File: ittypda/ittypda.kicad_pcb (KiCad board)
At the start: 2 copper layers, 105 x 109.8 mm, 172 parts, among them CN1 S2B-PH-SM4-TB, J1 USB_C_Receptacle_USB2.0_14P, J13 Conn_01x05_Pin, J14 Conn_01x05_Pin, J2 Conn_01x04_Pin, SW1 Switch, SW10 Switch, SW11 Switch, SW12 Switch, SW13 Switch, SW14 Switch, SW15 Switch, SW16 Switch, SW17 Switch, SW18 Switch, SW19 Switch, SW2 Switch, SW20 Switch, SW21 Switch, SW22 Switch, SW23 Switch, SW24 Switch, SW25 SLIDE SWITCH, SW26 Switch, SW27 Switch, SW28 Switch, SW29 Switch, SW3 Switch, SW30 Switch, SW31 Switch, SW32 Switch, SW33 Switch, SW34 Switch, SW36 Switch, SW37 Switch, SW38 Switch, SW39 Switch, SW4 Switch, SW41 Switch, SW42 Switch, SW43 Switch, SW44 Switch, SW45 Switch, SW46 Switch, SW47 Switch, SW48 Switch, SW49 Switch, SW5 Switch, SW50 Switch, SW51 Switch, SW52 Switch, SW53 Switch, SW54 Switch, SW55 Switch, SW56 Switch, SW57 Switch, SW58 Switch, SW59 Switch, SW6 Switch, SW60 Switch, SW61 Switch, SW7 Switch, SW8 Switch, SW9 Switch, U1 TPS63001, U2 BQ24040DSQR, U4 STM32F411RETx, Y1 16Mhz

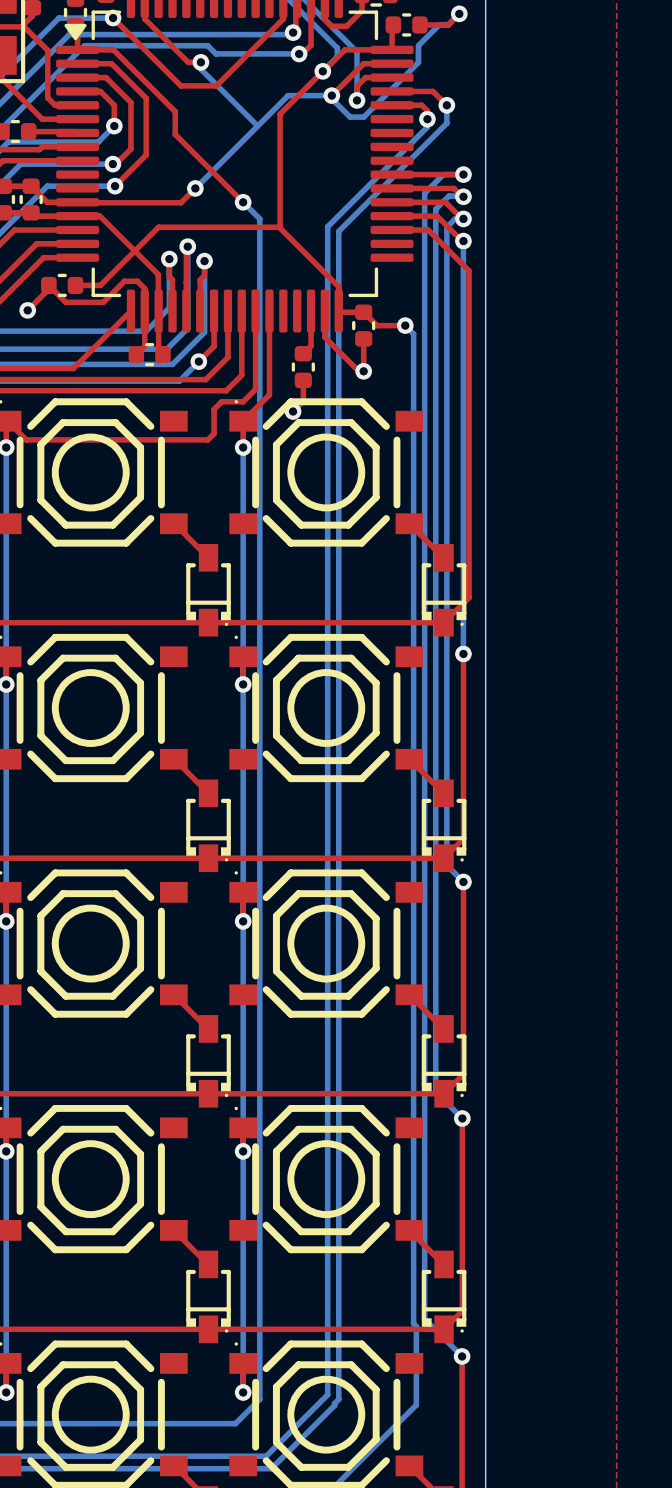
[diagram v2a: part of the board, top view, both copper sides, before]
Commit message: reorder row pins to reduce sharp angles
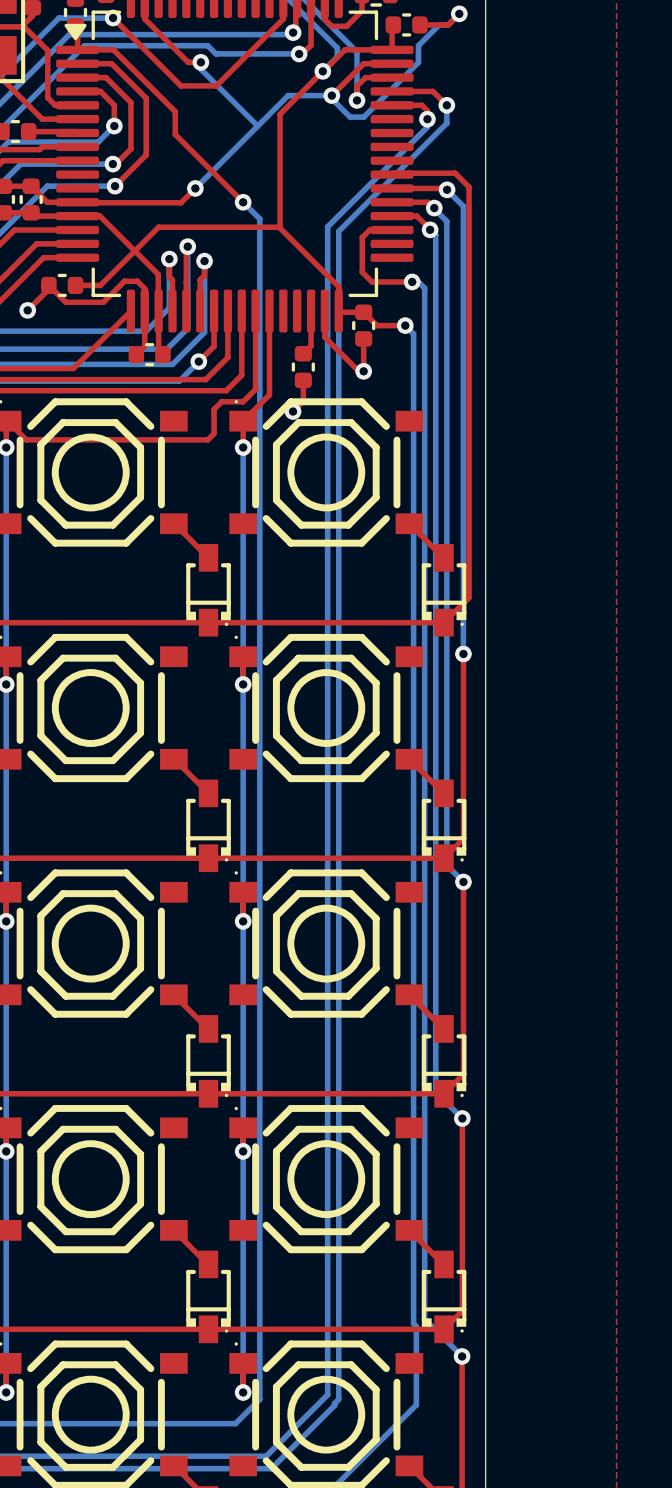
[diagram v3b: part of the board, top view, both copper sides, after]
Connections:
- U4 pad 35: Row0 -> Row4
- U4 pad 36: Row1 -> Row3
- U4 pad 38: Row3 -> Row1
- U4 pad 39: Row4 -> Row0
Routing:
- net Row3: track 138.6 -> 135.5 mm
- net Row0: track 110.0 -> 112.6 mm
- net Row4: track 147.8 -> 145.3 mm
- net Row1: track 119.0 -> 120.2 mm
- net Row2: track 128.9 -> 127.8 mm
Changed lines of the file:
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@@
 			(layers "F.Cu" "F.Mask" "F.Paste")
 			(roundrect_rratio 0.25)
-			(net "Row0")
+			(net "Row4")
 			(pinfunction "PB14_35")
 			(pintype "bidirectional")
@@
 			(layers "F.Cu" "F.Mask" "F.Paste")
 			(roundrect_rratio 0.25)
-			(net "Row1")
+			(net "Row3")
 			(pinfunction "PB15_36")
 			(pintype "bidirectional")
@@
 			(layers "F.Cu" "F.Mask" "F.Paste")
 			(roundrect_rratio 0.25)
-			(net "Row3")
+			(net "Row1")
 			(pinfunction "PC7_38")
 			(pintype "bidirectional")
@@
 			(layers "F.Cu" "F.Mask" "F.Paste")
 			(roundrect_rratio 0.25)
-			(net "Row4")
+			(net "Row0")
 			(pinfunction "PC8_39")
 			(pintype "bidirectional")
@@
 	)
 	(segment
+		(start 128.4 55.52)
+		(end 128.4 40.69964)
+		(width 0.2)
+		(layer "F.Cu")
+		(net "Row0")
+	)
+	(segment
 		(start 42.5 56.42)
 		(end 127.5 56.42)
@@
 	)
 	(segment
-		(start 128.4 55.52)
-		(end 128.4 43.725)
+		(start 127.5 56.42)
+		(end 128.4 55.52)
 		(width 0.2)
 		(layer "F.Cu")
@@
 	)
 	(segment
-		(start 126.925 42.25)
-		(end 125.625 42.25)
+		(start 125.675 40.2)
+		(end 125.625 40.25)
 		(width 0.2)
 		(layer "F.Cu")
@@
 	)
 	(segment
-		(start 128.4 43.725)
-		(end 126.925 42.25)
+		(start 127.90036 40.2)
+		(end 125.675 40.2)
 		(width 0.2)
 		(layer "F.Cu")
@@
 	)
 	(segment
-		(start 127.5 56.42)
-		(end 128.4 55.52)
+		(start 128.4 40.69964)
+		(end 127.90036 40.2)
 		(width 0.2)
 		(layer "F.Cu")
@@
 	)
 	(segment
-		(start 128.159823 81.260177)
-		(end 128.159823 74.312443)
-		(width 0.2)
-		(layer "F.Cu")
-		(net "Row3")
-	)
-	(segment
-		(start 127.851471 40.75)
-		(end 125.625 40.75)
+		(start 126.522013 41.75)
+		(end 125.625 41.75)
 		(width 0.2)
 		(layer "F.Cu")
@@
 	)
 	(segment
-		(start 127.5 81.92)
-		(end 128.159823 81.260177)
+		(start 127 42.240408)
+		(end 127 42.227987)
 		(width 0.2)
 		(layer "F.Cu")
@@
 	)
 	(segment
-		(start 128.2 41.050003)
-		(end 128.151474 41.050003)
+		(start 128.159823 81.260177)
+		(end 128.159823 74.312443)
 		(width 0.2)
 		(layer "F.Cu")
@@
 	)
 	(segment
-		(start 128.151474 41.050003)
-		(end 127.851471 40.75)
+		(start 127.5 81.92)
+		(end 128.159823 81.260177)
 		(width 0.2)
 		(layer "F.Cu")
@@
 	)
 	(segment
-		(start 128.2 41.050003)
-		(end 128.151476 41.098527)
+		(start 127 42.227987)
+		(end 126.522013 41.75)
 		(width 0.2)
 		(layer "F.Cu")
@@
 	)
 	(segment
-		(start 128.151476 41.098527)
-		(end 128.101473 41.098527)
+		(start 126.996599 42.243809)
+		(end 127 42.240408)
 		(width 0.2)
 		(layer "F.Cu")
@@
 	)
 	(via
-		(at 128.2 41.050003)
+		(at 126.996599 42.243809)
 		(size 0.6)
 		(drill 0.3)
@@
 	)
 	(segment
-		(start 127.675 41.025)
-		(end 128.174997 41.025)
+		(start 126.997244 42.244454)
+		(end 127.016467 42.244454)
 		(width 0.2)
 		(layer "B.Cu")
@@
 	)
 	(segment
-		(start 128.159823 74.312443)
+		(start 127.2 42.427987)
 		(end 127.2 73.35262)
 		(width 0.2)
@@
 	(segment
 		(start 127.2 73.35262)
-		(end 127.2 41.5)
+		(end 128.159823 74.312443)
 		(width 0.2)
 		(layer "B.Cu")
@@
 	)
 	(segment
-		(start 128.174997 41.025)
-		(end 128.2 41.050003)
+		(start 126.996599 42.243809)
+		(end 126.997244 42.244454)
 		(width 0.2)
 		(layer "B.Cu")
@@
 	)
 	(segment
-		(start 127.2 41.5)
-		(end 127.675 41.025)
+		(start 127.016467 42.244454)
+		(end 127.2 42.427987)
 		(width 0.2)
 		(layer "B.Cu")
@@
 	)
 	(segment
-		(start 128.2 40.25)
-		(end 125.8875 40.25)
+		(start 124.81759 42.25)
+		(end 125.625 42.25)
 		(width 0.2)
 		(layer "F.Cu")
@@
 	)
 	(segment
+		(start 124.55 42.51759)
+		(end 124.81759 42.25)
+		(width 0.2)
+		(layer "F.Cu")
+		(net "Row4")
+	)
+	(segment
 		(start 127.5 90.42)
 		(end 34 90.42)
@@
 		(net "Row4")
 	)
+	(segment
+		(start 124.55 43.775)
+		(end 124.55 42.51759)
+		(width 0.2)
+		(layer "F.Cu")
+		(net "Row4")
+	)
+	(segment
+		(start 126.35 44.125)
+		(end 124.9 44.125)
+		(width 0.2)
+		(layer "F.Cu")
+		(net "Row4")
+	)
+	(segment
+		(start 124.9 44.125)
+		(end 124.55 43.775)
+		(width 0.2)
+		(layer "F.Cu")
+		(net "Row4")
+	)
 	(via
 		(at 128.15 82.9)
@@
 	)
 	(via
-		(at 128.2 40.25)
+		(at 126.35 44.125)
 		(size 0.6)
 		(drill 0.3)
@@
 	)
 	(segment
-		(start 126.8 40.925)
-		(end 126.8 81.55)
+		(start 126.625 44.175)
+		(end 126.8 44.35)
 		(width 0.2)
 		(layer "B.Cu")
@@
 	)
 	(segment
-		(start 127.475 40.25)
-		(end 126.8 40.925)
+		(start 126.35 44.125)
+		(end 126.4 44.175)
 		(width 0.2)
 		(layer "B.Cu")
@@
 	)
 	(segment
-		(start 128.2 40.25)
-		(end 127.475 40.25)
+		(start 126.8 81.55)
+		(end 128.15 82.9)
 		(width 0.2)
 		(layer "B.Cu")
@@
 	)
 	(segment
-		(start 126.8 81.55)
-		(end 128.15 82.9)
+		(start 126.4 44.175)
+		(end 126.625 44.175)
+		(width 0.2)
+		(layer "B.Cu")
+		(net "Row4")
+	)
+	(segment
+		(start 126.8 44.35)
+		(end 126.8 81.55)
 		(width 0.2)
 		(layer "B.Cu")
@@
 	)
 	(segment
-		(start 127.551468 41.25)
-		(end 125.625 41.25)
+		(start 127.119089 41.458156)
+		(end 126.910933 41.25)
 		(width 0.2)
 		(layer "F.Cu")
@@
 	)
 	(segment
-		(start 128.151474 41.850006)
-		(end 127.551468 41.25)
+		(start 127.147443 41.458156)
+		(end 127.119089 41.458156)
 		(width 0.2)
 		(layer "F.Cu")
@@
 	)
 	(segment
-		(start 128.2 41.850006)
-		(end 128.151474 41.850006)
+		(start 127.5 73.42)
+		(end 34 73.42)
 		(width 0.2)
 		(layer "F.Cu")
@@
 	)
 	(segment
-		(start 127.5 73.42)
-		(end 34 73.42)
+		(start 126.910933 41.25)
+		(end 125.625 41.25)
 		(width 0.2)
 		(layer "F.Cu")
@@
 	)
 	(via
-		(at 128.2 41.850006)
+		(at 127.147443 41.458156)
 		(size 0.6)
 		(drill 0.3)
@@
 	(segment
 		(start 127.6 65.177071)
-		(end 127.6 42.15)
+		(end 128.2 65.777071)
 		(width 0.2)
 		(layer "B.Cu")
@@
 	)
 	(segment
-		(start 128.2 65.777071)
+		(start 127.6 41.939067)
 		(end 127.6 65.177071)
 		(width 0.2)
@@
 	)
 	(segment
-		(start 127.6 42.15)
-		(end 127.899994 41.850006)
+		(start 127.147443 41.458156)
+		(end 127.147443 41.48651)
 		(width 0.2)
 		(layer "B.Cu")
@@
 	)
 	(segment
-		(start 127.899994 41.850006)
-		(end 128.2 41.850006)
+		(start 127.147443 41.48651)
+		(end 127.6 41.939067)
 		(width 0.2)
 		(layer "B.Cu")
@@
 	)
 	(segment
-		(start 128.2 42.650009)
-		(end 128.150009 42.650009)
+		(start 127.609416 40.8)
+		(end 127.602191 40.8)
 		(width 0.2)
 		(layer "F.Cu")
@@
 	)
 	(segment
-		(start 128.150009 42.650009)
-		(end 127.25 41.75)
+		(start 127.602191 40.8)
+		(end 127.552191 40.75)
 		(width 0.2)
 		(layer "F.Cu")
@@
 	)
 	(segment
-		(start 127.25 41.75)
-		(end 125.625 41.75)
+		(start 128.2 64.22)
+		(end 128.2 57.55)
 		(width 0.2)
 		(layer "F.Cu")
@@
 	)
 	(segment
-		(start 128.2 64.22)
-		(end 128.2 57.55)
+		(start 127.552191 40.75)
+		(end 125.625 40.75)
 		(width 0.2)
 		(layer "F.Cu")
@@
 	)
 	(via
-		(at 128.2 42.650009)
+		(at 127.609416 40.8)
 		(size 0.6)
 		(drill 0.3)
@@
 	)
 	(segment
-		(start 128.2 57.55)
-		(end 128.2 42.650009)
+		(start 127.609416 40.8)
+		(end 127.609416 40.807225)
+		(width 0.2)
+		(layer "B.Cu")
+		(net "Row1")
+	)
+	(segment
+		(start 127.609416 40.807225)
+		(end 128.2 41.397809)
+		(width 0.2)
+		(layer "B.Cu")
+		(net "Row1")
+	)
+	(segment
+		(start 128.2 41.397809)
+		(end 128.2 57.55)
 		(width 0.2)
 		(layer "B.Cu")

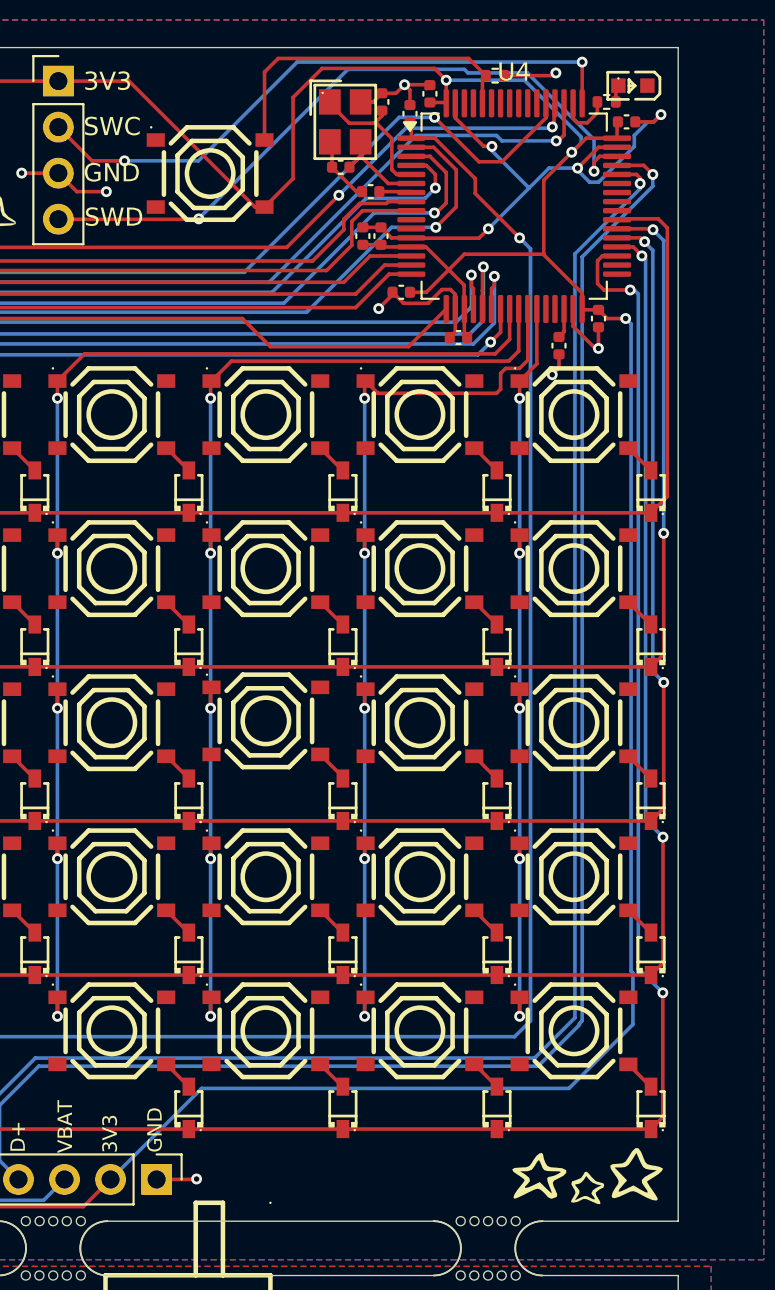
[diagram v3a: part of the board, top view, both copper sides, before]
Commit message: move decouplers to more optimal locations
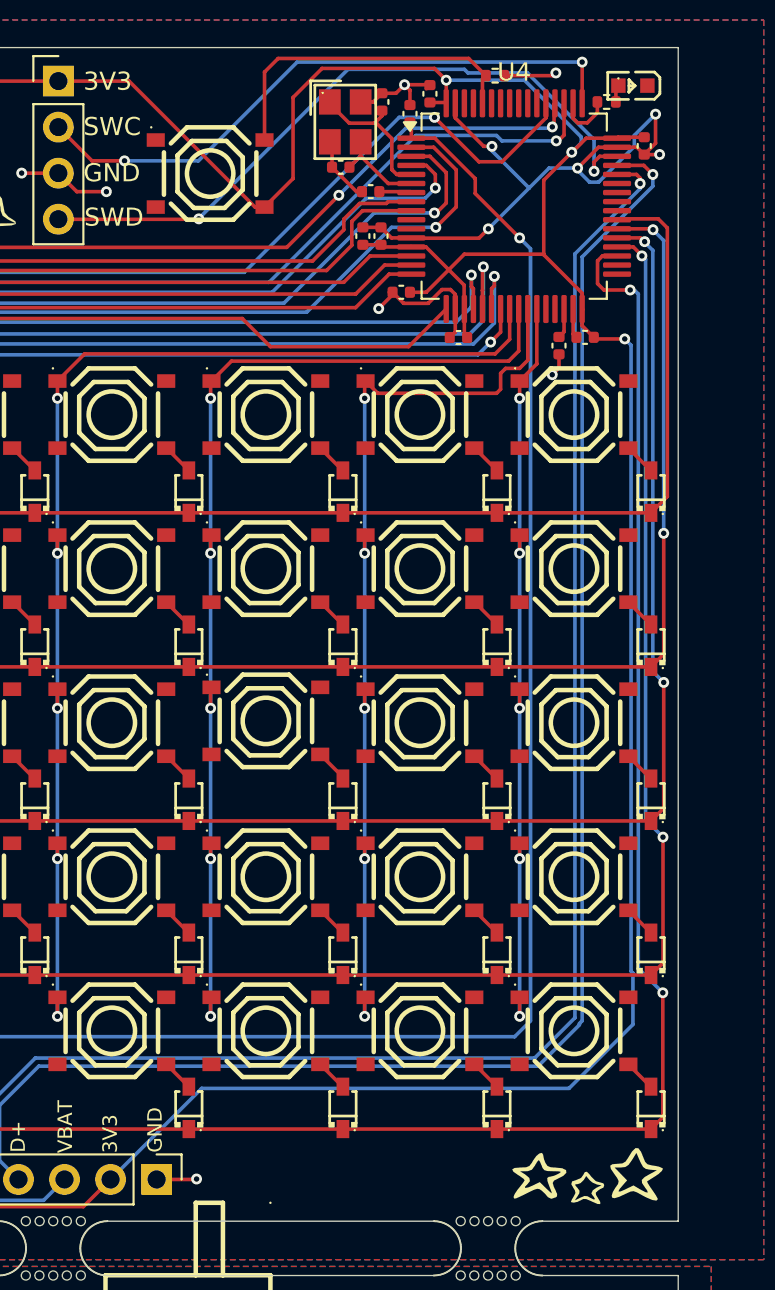
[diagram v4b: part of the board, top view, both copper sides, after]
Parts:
- moved C3 1.65 mm to (127.1, 36.2), turned to -90 degrees
- moved C2 1.27 mm to (123.9, 46.7), turned to 180 degrees
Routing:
- net GND: track 148.5 -> 149.3 mm
- net +3.3V: track 358.6 -> 359.1 mm

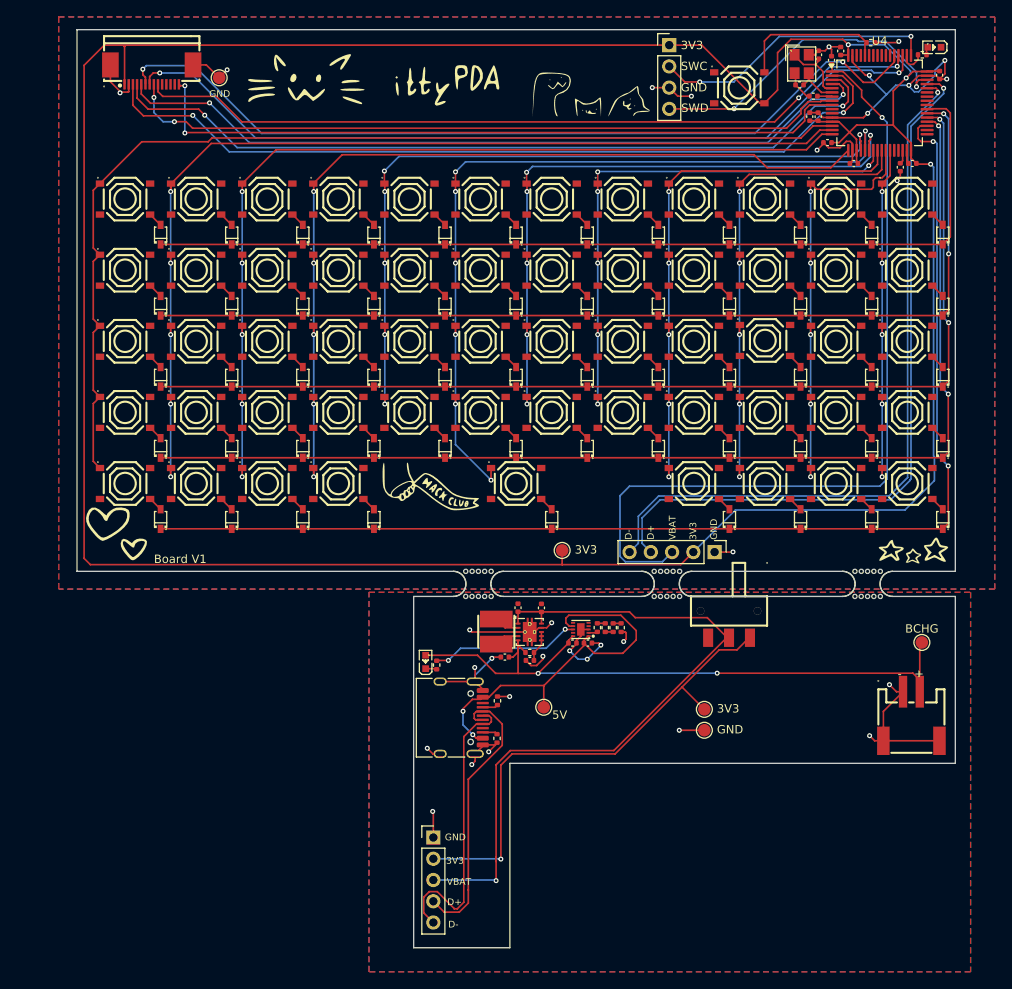
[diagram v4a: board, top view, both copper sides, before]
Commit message: add PCBA mounting holes to schematic
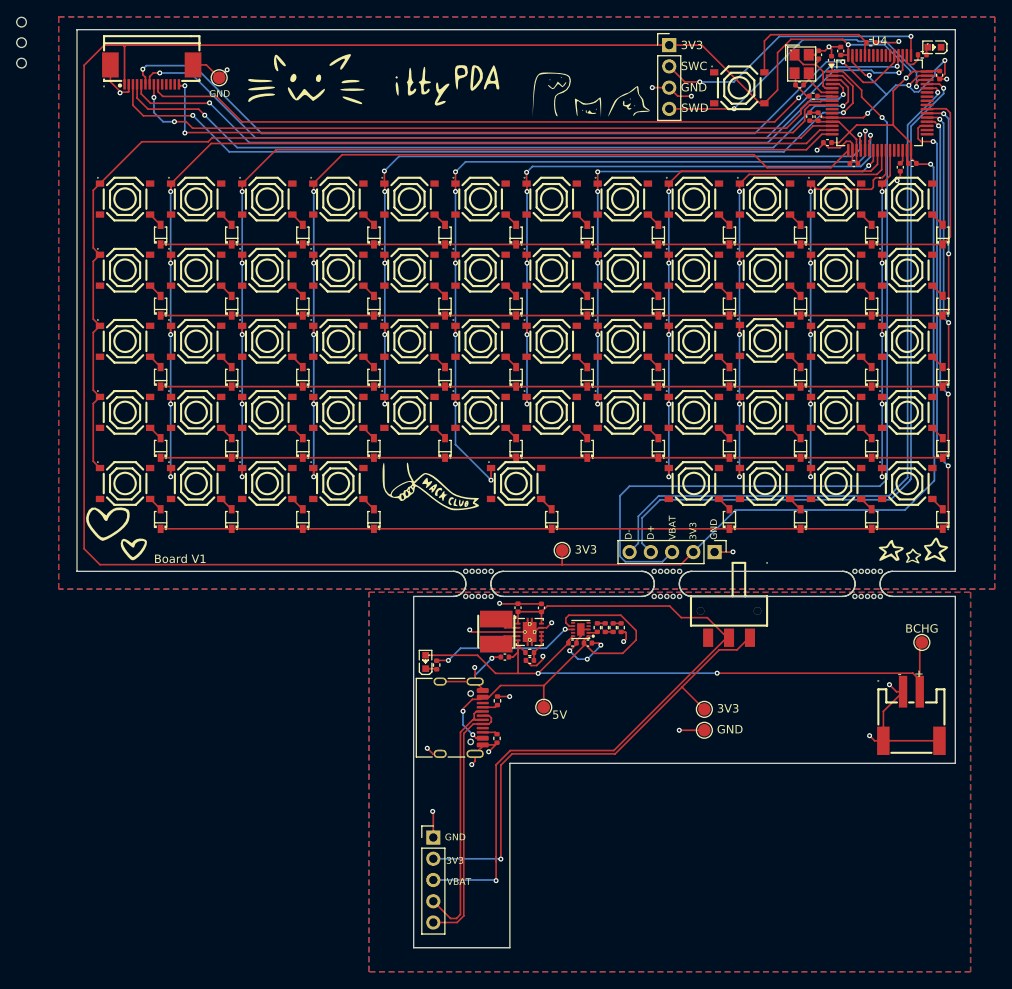
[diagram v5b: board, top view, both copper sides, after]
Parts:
- added H1: MountingHole, MountingHole:ToolingHole_1.152mm, F.Cu at (17.4, 29.9)
- added H2: MountingHole, MountingHole:ToolingHole_1.152mm, F.Cu at (17.4, 32.3)
- added H3: MountingHole, MountingHole:ToolingHole_1.152mm, F.Cu at (17.4, 34.8)
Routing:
- net GND: track 149.3 -> 154.3 mm, vias 31 -> 32
- net OutD-: track 35.2 -> 31.2 mm
- net OutD+: track 34.0 -> 31.3 mm
- net +3.3V: track 359.1 -> 358.4 mm
- net OutVBAT: track 84.6 -> 85.2 mm
